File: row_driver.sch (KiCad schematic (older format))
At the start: 23 parts, among them SW3 SW_PUSH_SMALL_H, SW4 SW_PUSH_SMALL_H, SW5 SW_PUSH_SMALL_H, SW6 SW_PUSH_SMALL_H, SW7 SW_PUSH_SMALL_H, SW8 SW_PUSH_SMALL_H, U11 74HC595, U13 74HC595, U15 74HC595, U23 CM1293A-04SO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

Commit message: Added stereo power amplifier
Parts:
- added C96: 1u, Capacitors_SMD:C_0603_HandSoldering, symbol device:C
- SW3, SW4, SW5, SW6, SW7, SW8: footprint components:SW_PUSH_6mm-2pin -> components:TACT_SW_SMD_Panasonic-EVPAWBD2A
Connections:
- net labels added: IRLED_K
- wire segments 144 -> 145
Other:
- note added: "place near TVSs"
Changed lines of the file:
@@
 $Descr A4 11693 8268
 encoding utf-8
-Sheet 5 10
+Sheet 5 11
 Title ""
 Date ""
@@
 F 0 "SW3" H 5850 2134 50  0000 C CNN
 F 1 "SW_PUSH_SMALL_H" H 5850 2134 50  0001 C CNN
-F 2 "components:SW_PUSH_6mm-2pin" H 5850 2200 50  0001 C CNN
+F 2 "components:TACT_SW_SMD_Panasonic-EVPAWBD2A" H 5850 2200 50  0001 C CNN
 F 3 "" H 5850 2200 50  0000 C CNN
 	1    5850 2000
@@
 F 0 "SW4" H 6200 1884 50  0000 C CNN
 F 1 "SW_PUSH_SMALL_H" H 6200 1884 50  0001 C CNN
-F 2 "components:SW_PUSH_6mm-2pin" H 6200 1950 50  0001 C CNN
+F 2 "components:TACT_SW_SMD_Panasonic-EVPAWBD2A" H 6200 1950 50  0001 C CNN
 F 3 "" H 6200 1950 50  0000 C CNN
 	1    6200 1750
@@
 F 0 "SW5" H 6200 2384 50  0000 C CNN
 F 1 "SW_PUSH_SMALL_H" H 6200 2384 50  0001 C CNN
-F 2 "components:SW_PUSH_6mm-2pin" H 6200 2450 50  0001 C CNN
+F 2 "components:TACT_SW_SMD_Panasonic-EVPAWBD2A" H 6200 2450 50  0001 C CNN
 F 3 "" H 6200 2450 50  0000 C CNN
 	1    6200 2250
@@
 F 0 "SW6" H 6650 2184 50  0000 C CNN
 F 1 "SW_PUSH_SMALL_H" H 6650 2184 50  0001 C CNN
-F 2 "components:SW_PUSH_6mm-2pin" H 6650 2250 50  0001 C CNN
+F 2 "components:TACT_SW_SMD_Panasonic-EVPAWBD2A" H 6650 2250 50  0001 C CNN
 F 3 "" H 6650 2250 50  0000 C CNN
 	1    6650 2050
@@
 F 0 "SW7" H 7200 2184 50  0000 C CNN
 F 1 "SW_PUSH_SMALL_H" H 7200 2184 50  0001 C CNN
-F 2 "components:SW_PUSH_6mm-2pin" H 7200 2250 50  0001 C CNN
+F 2 "components:TACT_SW_SMD_Panasonic-EVPAWBD2A" H 7200 2250 50  0001 C CNN
 F 3 "" H 7200 2250 50  0000 C CNN
 	1    7200 2050
@@
 F 0 "SW8" H 7700 2184 50  0000 C CNN
 F 1 "SW_PUSH_SMALL_H" H 7700 2184 50  0001 C CNN
-F 2 "components:SW_PUSH_6mm-2pin" H 7700 2250 50  0001 C CNN
+F 2 "components:TACT_SW_SMD_Panasonic-EVPAWBD2A" H 7700 2250 50  0001 C CNN
 F 3 "" H 7700 2250 50  0000 C CNN
 	1    7700 2050
@@
 	8050 2250 9250 2250
 Wire Wire Line
-	9550 3000 9500 3000
-Wire Wire Line
 	9300 3000 9300 2150
-Connection ~ 9500 3000
-Wire Wire Line
-	9500 3000 9300 3000
 Connection ~ 9300 2150
 Wire Wire Line
@@
 Wire Wire Line
 	9350 1650 10700 1650
+Wire Wire Line
+	9500 3000 9300 3000
+Text GLabel 10500 3200 2    50   Input ~ 0
+IRLED_K
+$Comp
+L device:C C96
+U 1 1 5BE4B4C9
+P 10600 3650
+F 0 "C96" H 10550 3100 50  0000 L CNN
+F 1 "1u" H 10550 3200 50  0000 L CNN
+F 2 "Capacitors_SMD:C_0603_HandSoldering" H 10715 3559 50  0001 L CNN
+F 3 "" H 10600 3650 50  0000 C CNN
+	1    10600 3650
+	1    0    0    -1
+$EndComp
+Text GLabel 10800 3400 3    60   Input ~ 0
+LEDLOGICVDD
+$Comp
+L power:GND #PWR05
+U 1 1 5BE52814
+P 10600 3800
+F 0 "#PWR05" H 10600 3550 50  0001 C CNN
+F 1 "GND" H 10605 3627 50  0000 C CNN
+F 2 "" H 10600 3800 50  0000 C CNN
+F 3 "" H 10600 3800 50  0000 C CNN
+	1    10600 3800
+	-1   0    0    -1
+$EndComp
+Wire Wire Line
+	10800 3400 10600 3400
+Wire Wire Line
+	10600 3400 10600 3500
+Text Notes 10250 4300 0    50   ~ 0
+place near TVSs
 $EndSCHEMATC

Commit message: Switched to new kicad libraries
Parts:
- C13, C14, C15, C96: symbol device:C -> dotmatrix_64x48-rescue:C-device
- D1, D2, D3, D4, D5, D6: symbol device:D_Schottky_Small -> dotmatrix_64x48-rescue:D_Schottky_Small-device
- R28, R47, R50: symbol device:R -> dotmatrix_64x48-rescue:R-device
- SW3, SW4, SW5, SW6, SW7, SW8: symbol Switch:SW_Push -> dotmatrix_64x48-rescue:SW_Push-Switch
- U23, U24: symbol ESD_Protection:SRV05-4 -> dotmatrix_64x48-rescue:SRV05-4-ESD_Protection
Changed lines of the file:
@@
 $EndSheet
 $Comp
-L Switch:SW_Push SW3
+L dotmatrix_64x48-rescue:SW_Push-Switch SW3
 U 1 1 58181DE2
 P 5850 2000
@@
 $EndComp
 $Comp
-L device:D_Schottky_Small D1
+L dotmatrix_64x48-rescue:D_Schottky_Small-device D1
 U 1 1 58182A5C
 P 10500 1750
@@
 SEL1
 $Comp
-L Switch:SW_Push SW4
+L dotmatrix_64x48-rescue:SW_Push-Switch SW4
 U 1 1 58183FA7
 P 6200 1750
@@
 $EndComp
 $Comp
-L device:D_Schottky_Small D2
+L dotmatrix_64x48-rescue:D_Schottky_Small-device D2
 U 1 1 58183FAD
 P 10500 1850
@@
 SEL2
 $Comp
-L Switch:SW_Push SW5
+L dotmatrix_64x48-rescue:SW_Push-Switch SW5
 U 1 1 58184034
 P 6200 2250
@@
 $EndComp
 $Comp
-L device:D_Schottky_Small D3
+L dotmatrix_64x48-rescue:D_Schottky_Small-device D3
 U 1 1 5818403A
 P 10500 1950
@@
 SEL3
 $Comp
-L Switch:SW_Push SW6
+L dotmatrix_64x48-rescue:SW_Push-Switch SW6
 U 1 1 58184145
 P 6650 2050
@@
 $EndComp
 $Comp
-L device:D_Schottky_Small D4
+L dotmatrix_64x48-rescue:D_Schottky_Small-device D4
 U 1 1 5818414B
 P 10500 2050
@@
 SEL4
 $Comp
-L Switch:SW_Push SW7
+L dotmatrix_64x48-rescue:SW_Push-Switch SW7
 U 1 1 58184270
 P 7200 2050
@@
 $EndComp
 $Comp
-L device:D_Schottky_Small D5
+L dotmatrix_64x48-rescue:D_Schottky_Small-device D5
 U 1 1 58184276
 P 10500 2150
@@
 SEL5
 $Comp
-L Switch:SW_Push SW8
+L dotmatrix_64x48-rescue:SW_Push-Switch SW8
 U 1 1 58184403
 P 7700 2050
@@
 $EndComp
 $Comp
-L device:D_Schottky_Small D6
+L dotmatrix_64x48-rescue:D_Schottky_Small-device D6
 U 1 1 58184409
 P 10500 2250
@@
 BUTTONSENSE
 $Comp
-L device:R R28
+L dotmatrix_64x48-rescue:R-device R28
 U 1 1 58185F31
 P 10700 1250
@@
 $EndComp
 $Comp
-L device:C C14
+L dotmatrix_64x48-rescue:C-device C14
 U 1 1 58184665
 P 6950 5100
@@
 $EndComp
 $Comp
-L device:C C15
+L dotmatrix_64x48-rescue:C-device C15
 U 1 1 58184673
 P 7250 5100
@@
 $EndComp
 $Comp
-L device:R R47
+L dotmatrix_64x48-rescue:R-device R47
 U 1 1 582610FB
 P 1900 5100
@@
 $EndComp
 $Comp
-L device:C C13
+L dotmatrix_64x48-rescue:C-device C13
 U 1 1 58184657
 P 6650 5100
@@
 $EndComp
 $Comp
-L power:GND #PWR086
+L dotmatrix_64x48-rescue:GND-power #PWR086
 U 1 1 5943AB4A
 P 6650 5250
@@
 $EndComp
 $Comp
-L power:GND #PWR087
+L dotmatrix_64x48-rescue:GND-power #PWR087
 U 1 1 5943AB76
 P 6950 5250
@@
 $EndComp
 $Comp
-L power:GND #PWR088
+L dotmatrix_64x48-rescue:GND-power #PWR088
 U 1 1 5943ABA2
 P 7250 5250
@@
 $EndComp
 $Comp
-L power:GND #PWR080
+L dotmatrix_64x48-rescue:GND-power #PWR080
 U 1 1 5943B74E
 P 4300 4450
@@
 $EndComp
 $Comp
-L power:GND #PWR078
+L dotmatrix_64x48-rescue:GND-power #PWR078
 U 1 1 5943B77A
 P 4000 4450
@@
 $EndComp
 $Comp
-L power:GND #PWR077
+L dotmatrix_64x48-rescue:GND-power #PWR077
 U 1 1 5943B994
 P 2950 4450
@@
 $EndComp
 $Comp
-L power:GND #PWR075
+L dotmatrix_64x48-rescue:GND-power #PWR075
 U 1 1 5943B9C0
 P 2650 4450
@@
 $EndComp
 $Comp
-L power:GND #PWR074
+L dotmatrix_64x48-rescue:GND-power #PWR074
 U 1 1 5943B9EC
 P 1600 4450
@@
 $EndComp
 $Comp
-L power:GND #PWR072
+L dotmatrix_64x48-rescue:GND-power #PWR072
 U 1 1 5943BA18
 P 1300 4450
@@
 	10700 1000 10500 1000
 $Comp
-L device:R R50
+L dotmatrix_64x48-rescue:R-device R50
 U 1 1 59E6F4DB
 P 5400 1800
@@
 $EndComp
 $Comp
-L power:GND #PWR0160
+L dotmatrix_64x48-rescue:GND-power #PWR0160
 U 1 1 59E6F925
 P 5400 2200
@@
 Connection ~ 3050 5800
 $Comp
-L ESD_Protection:SRV05-4 U23
+L dotmatrix_64x48-rescue:SRV05-4-ESD_Protection U23
 U 1 1 5C37A961
 P 8650 3100
@@
 Connection ~ 7500 1650
 $Comp
-L power:GND #PWR0132
+L dotmatrix_64x48-rescue:GND-power #PWR0132
 U 1 1 5C3A7031
 P 8650 3600
@@
 	9200 2050 10400 2050
 $Comp
-L ESD_Protection:SRV05-4 U24
+L dotmatrix_64x48-rescue:SRV05-4-ESD_Protection U24
 U 1 1 5C3C9D6E
 P 10000 3100
@@
 $EndComp
 $Comp
-L power:GND #PWR0133
+L dotmatrix_64x48-rescue:GND-power #PWR0133
 U 1 1 5C3C9D74
 P 10000 3600
@@
 IRLED_K
 $Comp
-L device:C C96
+L dotmatrix_64x48-rescue:C-device C96
 U 1 1 5BE4B4C9
 P 10600 3650
@@
 LEDLOGICVDD
 $Comp
-L power:GND #PWR05
+L dotmatrix_64x48-rescue:GND-power #PWR05
 U 1 1 5BE52814
 P 10600 3800

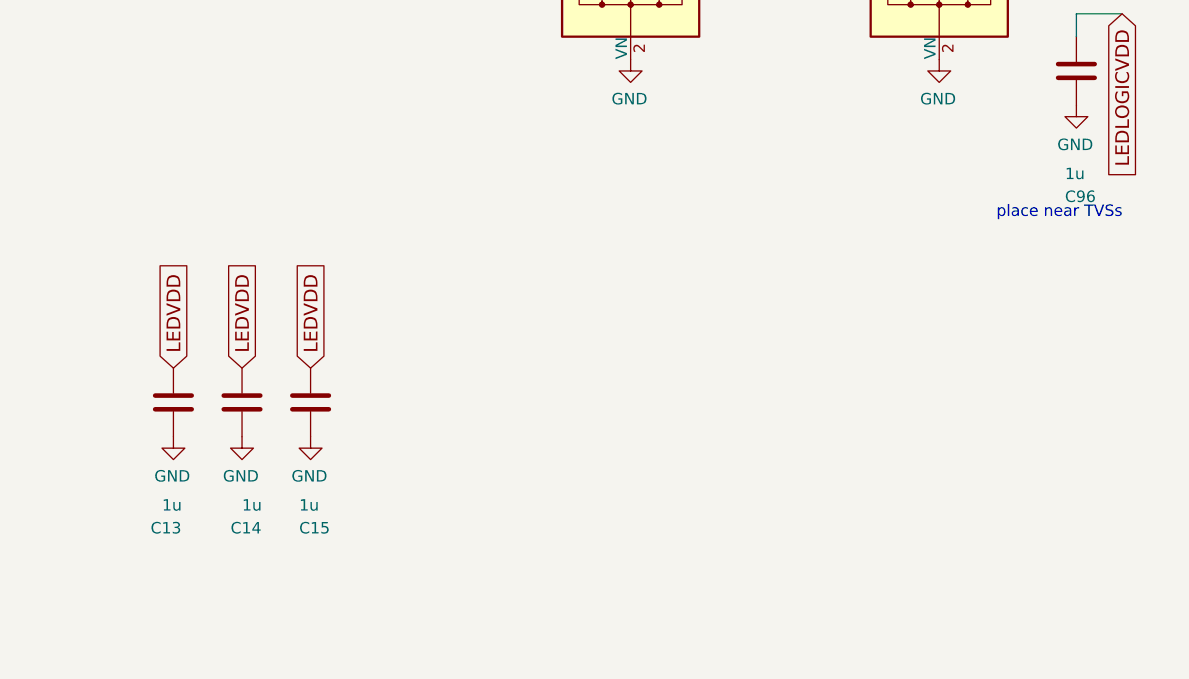
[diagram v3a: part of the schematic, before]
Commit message: Changed footprints from old 4.x's R/C to 5.x's
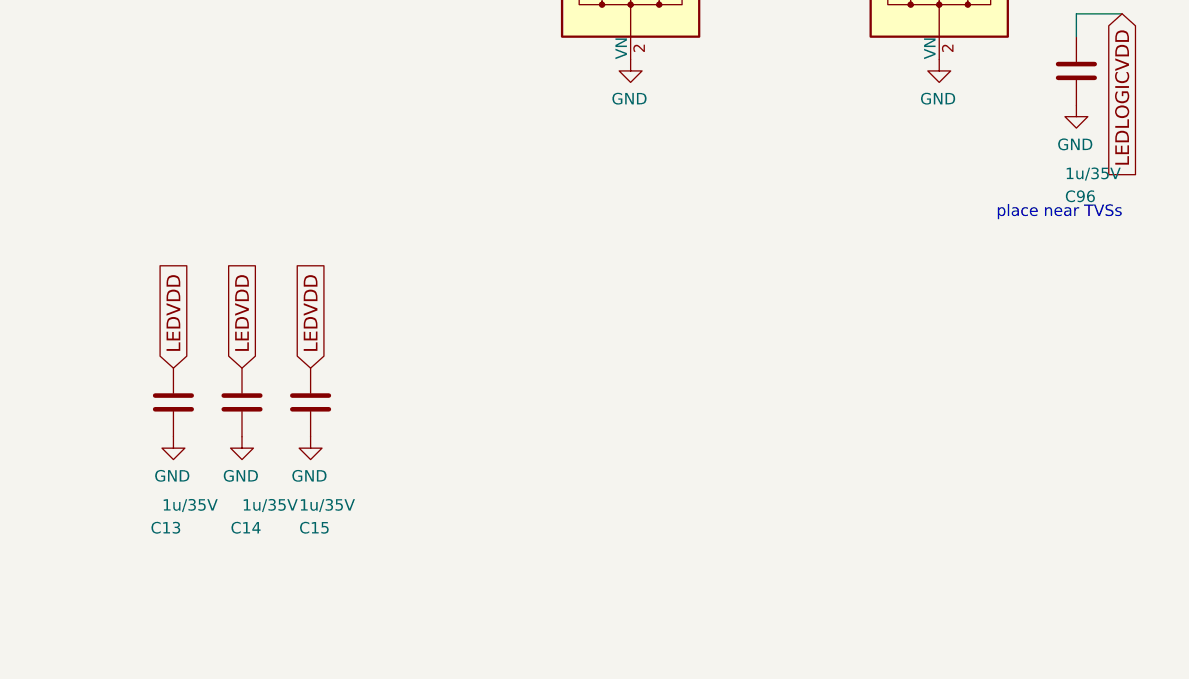
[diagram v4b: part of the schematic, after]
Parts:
- C13, C14, C15, C96: value 1u -> 1u/35V; footprint Capacitors_SMD:C_0603_HandSoldering -> Capacitor_SMD:C_0603_1608Metric_Pad1.05x0.95mm_HandSolder
- R28, R47, R50: footprint Resistors_SMD:R_0603_HandSoldering -> Resistor_SMD:R_0603_1608Metric_Pad1.05x0.95mm_HandSolder
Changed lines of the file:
@@
 F 0 "R28" V 10700 1200 50  0000 L CNN
 F 1 "10k" V 10750 950 50  0000 L CNN
-F 2 "Resistors_SMD:R_0603_HandSoldering" V 10630 1250 50  0001 C CNN
+F 2 "Resistor_SMD:R_0603_1608Metric_Pad1.05x0.95mm_HandSolder" V 10630 1250 50  0001 C CNN
 F 3 "" H 10700 1250 50  0000 C CNN
 	1    10700 1250
@@
 P 6950 5100
 F 0 "C14" H 6900 4550 50  0000 L CNN
-F 1 "1u" H 6950 4650 50  0000 L CNN
-F 2 "Capacitors_SMD:C_0603_HandSoldering" H 7065 5009 50  0001 L CNN
+F 1 "1u/35V" H 6950 4650 50  0000 L CNN
+F 2 "Capacitor_SMD:C_0603_1608Metric_Pad1.05x0.95mm_HandSolder" H 7065 5009 50  0001 L CNN
 F 3 "" H 6950 5100 50  0000 C CNN
 	1    6950 5100
@@
 P 7250 5100
 F 0 "C15" H 7200 4550 50  0000 L CNN
-F 1 "1u" H 7200 4650 50  0000 L CNN
-F 2 "Capacitors_SMD:C_0603_HandSoldering" H 7365 5009 50  0001 L CNN
+F 1 "1u/35V" H 7200 4650 50  0000 L CNN
+F 2 "Capacitor_SMD:C_0603_1608Metric_Pad1.05x0.95mm_HandSolder" H 7365 5009 50  0001 L CNN
 F 3 "" H 7250 5100 50  0000 C CNN
 	1    7250 5100
@@
 F 0 "R47" V 1900 5000 50  0000 L CNN
 F 1 "4.7k" V 1800 5100 50  0000 L CNN
-F 2 "Resistors_SMD:R_0603_HandSoldering" V 1830 5100 50  0001 C CNN
+F 2 "Resistor_SMD:R_0603_1608Metric_Pad1.05x0.95mm_HandSolder" V 1830 5100 50  0001 C CNN
 F 3 "" H 1900 5100 50  0000 C CNN
 	1    1900 5100
@@
 P 6650 5100
 F 0 "C13" H 6550 4550 50  0000 L CNN
-F 1 "1u" H 6600 4650 50  0000 L CNN
-F 2 "Capacitors_SMD:C_0603_HandSoldering" H 6765 5009 50  0001 L CNN
+F 1 "1u/35V" H 6600 4650 50  0000 L CNN
+F 2 "Capacitor_SMD:C_0603_1608Metric_Pad1.05x0.95mm_HandSolder" H 6765 5009 50  0001 L CNN
 F 3 "" H 6650 5100 50  0000 C CNN
 	1    6650 5100
@@
 F 0 "R50" V 5400 1750 50  0000 L CNN
 F 1 "10k DNI" V 5500 1600 50  0000 L CNN
-F 2 "Resistors_SMD:R_0603_HandSoldering" V 5330 1800 50  0001 C CNN
+F 2 "Resistor_SMD:R_0603_1608Metric_Pad1.05x0.95mm_HandSolder" V 5330 1800 50  0001 C CNN
 F 3 "" H 5400 1800 50  0000 C CNN
 	1    5400 1800
@@
 P 10600 3650
 F 0 "C96" H 10550 3100 50  0000 L CNN
-F 1 "1u" H 10550 3200 50  0000 L CNN
-F 2 "Capacitors_SMD:C_0603_HandSoldering" H 10715 3559 50  0001 L CNN
+F 1 "1u/35V" H 10550 3200 50  0000 L CNN
+F 2 "Capacitor_SMD:C_0603_1608Metric_Pad1.05x0.95mm_HandSolder" H 10715 3559 50  0001 L CNN
 F 3 "" H 10600 3650 50  0000 C CNN
 	1    10600 3650
